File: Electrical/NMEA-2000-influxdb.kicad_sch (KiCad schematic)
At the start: 10 parts, among them J1 Conn_01x02, J3 Conn_01x02, U1 LM7805_TO220, U3 RTC-Module, U4 ESP32-DevKitC, U5 SD-Card-Module, U6 SN65HVD230

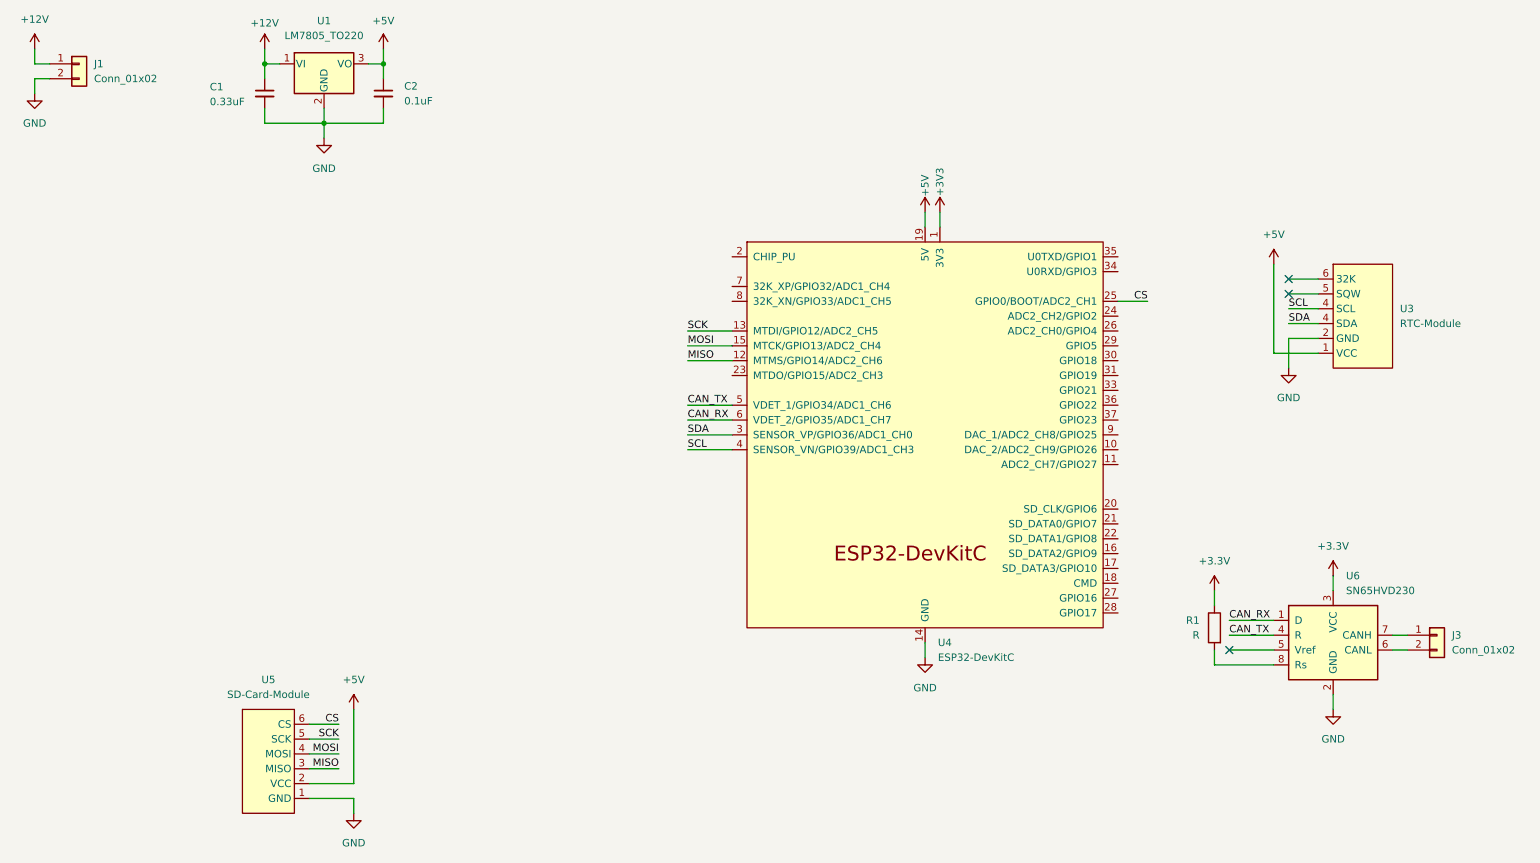
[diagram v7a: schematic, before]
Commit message: Replaced SN65HVD230-Module with SN65HVD230
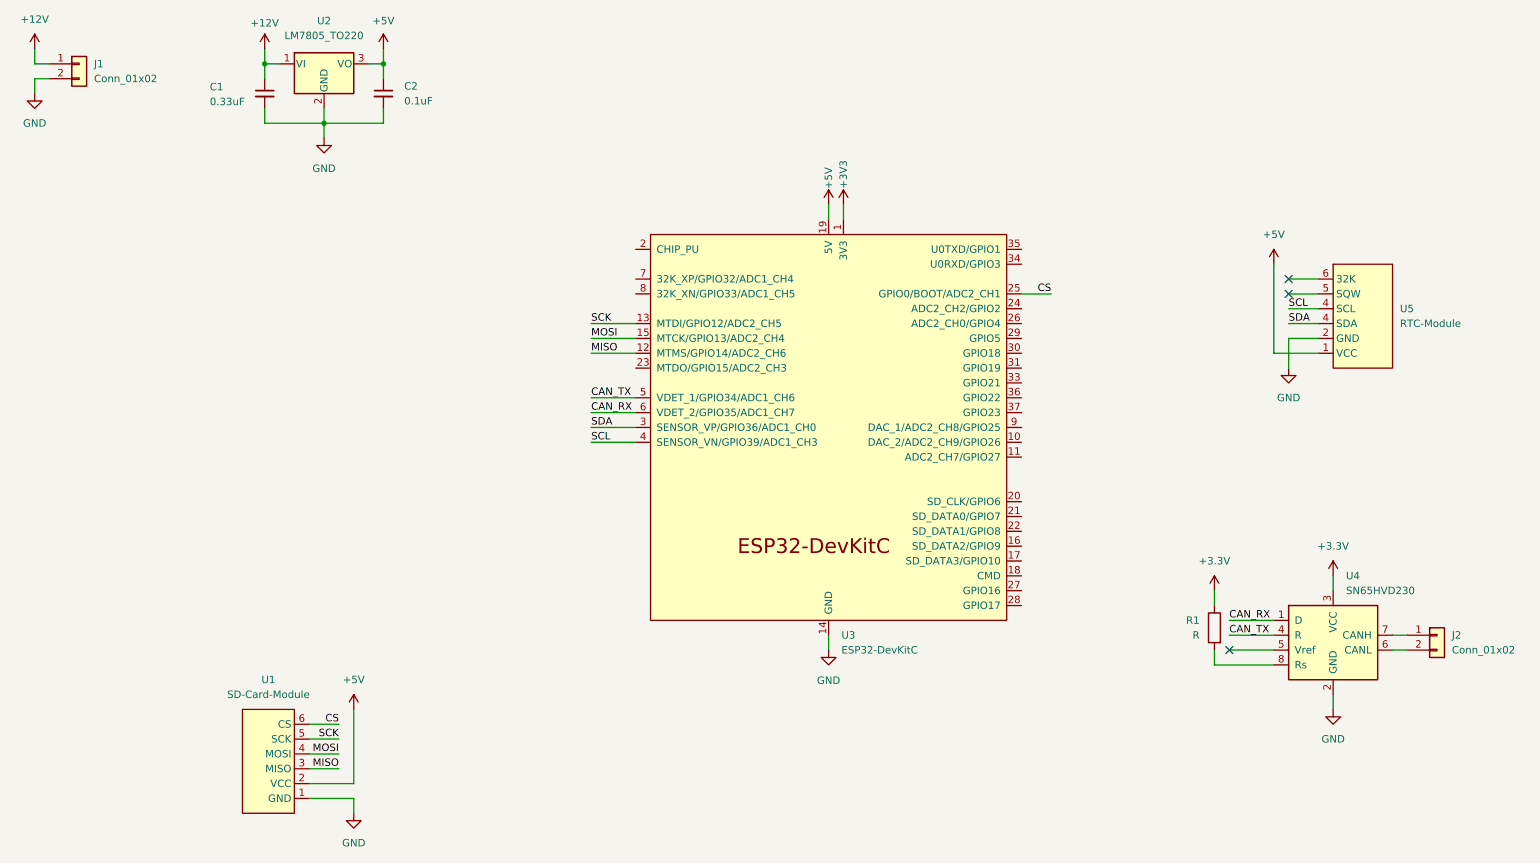
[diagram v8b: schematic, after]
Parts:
- J2: renamed from J3; footprint (none) -> TerminalBlock_Phoenix:TerminalBlock_Phoenix_MKDS-1,5-2-5.08_1x02_P5.08mm_Horizontal
- R1: footprint (none) -> Resistor_THT:R_Axial_DIN0204_L3.6mm_D1.6mm_P5.08mm_Horizontal
- renumbered U5 to U1, U1 to U2, U4 to U3, U6 to U4, U3 to U5
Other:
- moved on the sheet: U3
